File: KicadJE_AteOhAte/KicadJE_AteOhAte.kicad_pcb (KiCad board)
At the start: 2 copper layers, 100 x 100 mm, 180 parts, among them J201 In_Accent, J202 In Gate, J203 Out Tom, J301 Out 1, J302 In_1, J303 Out 2, J304 In 2, J305 Out 1 Final, J306 Out 2 Final, P201 Doepfer_Power_10pin, Q201 MMBT2222A, Q202 MMBT2222A, Q203 MMBT2222A, Q204 MMBT2222A, Q205 MMBT2907A, Q206 MMBT2222A, Q207 MMBT2222A, SW201 Con/Tom, U201 TL072, U202 TL072, U203 TL072, U301 TL072, U302 TL072

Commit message: PCB
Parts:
- removed C313, C314: 1u, Capacitor_SMD:C_0805_2012Metric_Pad1.15x1.40mm_HandSolder
- removed D311, D312: D_Zener, Diode_SMD:D_MiniMELF
- removed J301: Out 1, AJ-Dropbox-Kicad:PJ301SM
- removed J302: In_1, AJ-Dropbox-Kicad:PJ301SM
- removed J303: Out 2, AJ-Dropbox-Kicad:PJ301SM
- removed J304: In 2, AJ-Dropbox-Kicad:PJ301SM
- removed J305: Out 1 Final, AJ-Dropbox-Kicad:PJ301SM
- removed J306: Out 2 Final, AJ-Dropbox-Kicad:PJ301SM
- added H203: 2,2mm, MountingHole:MountingHole_2.2mm_M2_Pad_Via, F.Cu at (160.0, 53.5)
- D204: value Zener -> D_Zener
- moved D306 46.8 mm to (144.0, 33.9)
- moved D305 46.1 mm to (137.7, 33.9)
- moved C305 45.9 mm to (173.0, 52.0)
- moved R310 44.5 mm to (153.9, 39.5)
- moved R301 43.3 mm to (154.3, 33.6)
- moved D303 41.6 mm to (142.5, 38.3)
- moved C307 40.8 mm to (177.7, 52.0)
- moved C306 38.1 mm to (160.3, 24.2)
- moved C310 36.1 mm to (136.9, 40.2)
- moved R317 33.8 mm to (163.8, 33.0)
- moved R325 33.3 mm to (168.1, 36.0)
- moved D304 32.9 mm to (148.4, 21.6)
- moved C308 30.6 mm to (124.2, 44.7)
- moved R312 30.6 mm to (129.0, 44.7)
- moved U302 30.5 mm to (139.9, 20.6)
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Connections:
- net /KicadJE_AteOhAte3/POT1_C renamed Net-(R301-Pad2)
- net /KicadJE_AteOhAte3/POT1_L renamed Net-(C301-Pad1)
- net /KicadJE_AteOhAte3/POT2_L renamed Net-(R303-Pad1)
- net /KicadJE_AteOhAte3/POT3_C renamed Net-(R312-Pad1)
- net /KicadJE_AteOhAte3/POT4_C renamed Net-(R319-Pad2)
- C305 pad 1: Net-(C305-Pad1) -> (no net)
- C305 pad 2: Out1_Dist -> (no net)
- C306 pad 2: In_1 -> (no net)
- C307 pad 1: Net-(C307-Pad1) -> (no net)
- C307 pad 2: Out2_Dist -> (no net)
- C310 pad 2: In_2 -> (no net)
- R307 pad 2: In_1 -> (no net)
- R311 pad 2: Out1_Dist -> (no net)
- R317 pad 2: In_2 -> (no net)
- R322 pad 2: Out2_Dist -> (no net)
- R327 pad 1: Net-(J302-PadT) -> (no net)
- R329 pad 1: Net-(J302-PadTN) -> (no net)

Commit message: Fused RIAA SCH
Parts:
- removed D303, D310: LED, LED_THT:LED_D3.0mm
- removed D305, D306, D307, D308, D309: LL4148, Diode_SMD:D_MiniMELF
- added C313: 470n, Capacitor_SMD:C_0805_2012Metric_Pad1.15x1.40mm_HandSolder, B.Cu at (208.3, 122.9)
- added C314: 470n_THT, Capacitor_THT:C_Rect_L7.2mm_W5.5mm_P5.00mm_FKS2_FKP2_MKS2_MKP2, F.Cu at (182.0, 87.3)
- added C315: 470n_THT, Capacitor_THT:C_Rect_L7.2mm_W5.5mm_P5.00mm_FKS2_FKP2_MKS2_MKP2, F.Cu at (186.2, 50.8)
- added C316: 100u, Capacitor_SMD:CP_Elec_8x6.5, F.Cu at (158.0, 66.0)
- added C317: 2n2_THT, Capacitor_THT:C_Rect_L7.2mm_W5.5mm_P5.00mm_FKS2_FKP2_MKS2_MKP2, F.Cu at (189.1, 60.7)
- added C318: 47p, Capacitor_SMD:C_0805_2012Metric_Pad1.15x1.40mm_HandSolder, B.Cu at (202.7, 110.8)
- added C319: 2n2, Capacitor_SMD:C_0805_2012Metric_Pad1.15x1.40mm_HandSolder, B.Cu at (226.6, 134.5)
- added C320: 1n_THT, Capacitor_THT:C_Rect_L7.2mm_W5.5mm_P5.00mm_FKS2_FKP2_MKS2_MKP2, F.Cu at (164.5, 87.3)
- added C321: 680p_THT, Capacitor_THT:C_Rect_L7.2mm_W5.5mm_P5.00mm_FKS2_FKP2_MKS2_MKP2, F.Cu at (199.8, 52.9)
- added C322: 47p, Capacitor_SMD:C_0805_2012Metric_Pad1.15x1.40mm_HandSolder, B.Cu at (183.7, 111.7)
- added C323: 1n, Capacitor_SMD:C_0805_2012Metric_Pad1.15x1.40mm_HandSolder, B.Cu at (188.5, 110.7)
- added C324: 680p, Capacitor_SMD:C_0805_2012Metric_Pad1.15x1.40mm_HandSolder, B.Cu at (193.2, 113.6)
- added C325: 470n_THT, Capacitor_THT:C_Rect_L7.2mm_W5.5mm_P5.00mm_FKS2_FKP2_MKS2_MKP2, F.Cu at (208.6, 52.9)
- added C326: 470n, Capacitor_SMD:C_1206_3216Metric_Pad1.42x1.75mm_HandSolder, B.Cu at (192.4, 123.2)
- added C327: 470n, Capacitor_SMD:C_0805_2012Metric_Pad1.15x1.40mm_HandSolder, B.Cu at (212.4, 132.5)
- added C328: 470n, Capacitor_SMD:C_0805_2012Metric_Pad1.15x1.40mm_HandSolder, B.Cu at (198.8, 120.4)
- added C329: 470n_THT, Capacitor_THT:C_Rect_L7.2mm_W5.5mm_P5.00mm_FKS2_FKP2_MKS2_MKP2, F.Cu at (197.9, 60.7)
- added C330: 470n_THT, Capacitor_THT:C_Rect_L7.2mm_W5.5mm_P5.00mm_FKS2_FKP2_MKS2_MKP2, F.Cu at (167.4, 52.5)
- added C331: 10u, Capacitor_THT:CP_Radial_D8.0mm_P3.50mm, F.Cu at (184.8, 74.8)
- added C332: 22u, Capacitor_THT:CP_Radial_D8.0mm_P3.50mm, F.Cu at (163.8, 75.2)
- added C333: 10u, Capacitor_SMD:C_0805_2012Metric_Pad1.15x1.40mm_HandSolder, B.Cu at (221.9, 143.4)
- added C334: 1u, Capacitor_SMD:C_0805_2012Metric_Pad1.15x1.40mm_HandSolder, B.Cu at (202.5, 125.5)
- added C335: 100n, Capacitor_SMD:C_0805_2012Metric_Pad1.15x1.40mm_HandSolder, B.Cu at (177.4, 108.5)
- added C336: 100n, Capacitor_SMD:C_0805_2012Metric_Pad1.15x1.40mm_HandSolder, B.Cu at (212.4, 135.5)
- added C337: 100n, Capacitor_SMD:C_0805_2012Metric_Pad1.15x1.40mm_HandSolder, B.Cu at (188.5, 113.6)
- added C338: 100n, Capacitor_SMD:C_0805_2012Metric_Pad1.15x1.40mm_HandSolder, B.Cu at (221.9, 146.3)
- added C339: 100n, Capacitor_SMD:C_0805_2012Metric_Pad1.15x1.40mm_HandSolder, B.Cu at (226.7, 149.3)
- added C340: 100n, Capacitor_SMD:C_0805_2012Metric_Pad1.15x1.40mm_HandSolder, B.Cu at (215.2, 138.5)
- added C341: 10u, Capacitor_SMD:C_0805_2012Metric_Pad1.15x1.40mm_HandSolder, B.Cu at (194.0, 117.1)
- added C342: 1u, Capacitor_SMD:C_0805_2012Metric_Pad1.15x1.40mm_HandSolder, B.Cu at (198.0, 111.6)
- added C343: 10u, Capacitor_THT:CP_Radial_D8.0mm_P3.50mm, F.Cu at (175.0, 75.2)
- added C344: 22u, Capacitor_THT:CP_Radial_D8.0mm_P3.50mm, F.Cu at (195.5, 75.5)
- added C345: 470u, Capacitor_THT:CP_Radial_D13.0mm_P5.00mm, F.Cu at (116.0, 65.5)
- added C346: 470u, Capacitor_THT:CP_Radial_D13.0mm_P5.00mm, F.Cu at (116.0, 79.0)
- added J301: PJRAS2X2S01AUX, AJ:PJRAS2X2S01AUX_RCA, F.Cu at (141.0, 119.8)
- added J302: Conn_01x03, TerminalBlock:TerminalBlock_bornier-3_P5.08mm, F.Cu at (105.0, 79.5)
- added U303: TL072, AJ-Dropbox-Kicad:AJ_SO-8_5.3x6.2mm_P1.27mm, B.Cu at (167.2, 116.5)
- C301: value 10n -> 2n2_THT; footprint Capacitor_SMD:C_0805_2012Metric_Pad1.15x1.40mm_HandSolder -> Capacitor_THT:C_Rect_L7.2mm_W5.5mm_P5.00mm_FKS2_FKP2_MKS2_MKP2
- C302: value 10n -> 100u; footprint Capacitor_SMD:C_0805_2012Metric_Pad1.15x1.40mm_HandSolder -> Capacitor_SMD:CP_Elec_8x6.5
- C303: value 10n -> 2n2; moved to B.Cu
- C304: value 10n -> 1n_THT; footprint Capacitor_SMD:C_0805_2012Metric_Pad1.15x1.40mm_HandSolder -> Capacitor_THT:C_Rect_L7.2mm_W5.5mm_P5.00mm_FKS2_FKP2_MKS2_MKP2
- C305: value 1u -> 680p_THT; footprint Capacitor_SMD:C_0805_2012Metric_Pad1.15x1.40mm_HandSolder -> Capacitor_THT:C_Rect_L7.2mm_W5.5mm_P5.00mm_FKS2_FKP2_MKS2_MKP2
- C306, C310: value 1u -> 47p; moved to B.Cu
- C307: value 1u -> 1n; moved to B.Cu
- C308: value 100n -> 680p; moved to B.Cu
- C309: value 100n -> 470n_THT; footprint Capacitor_SMD:C_0805_2012Metric_Pad1.15x1.40mm_HandSolder -> Capacitor_THT:C_Rect_L7.2mm_W5.5mm_P5.00mm_FKS2_FKP2_MKS2_MKP2
- C311: value 100n -> 470n; footprint Capacitor_SMD:C_0805_2012Metric_Pad1.15x1.40mm_HandSolder -> Capacitor_SMD:C_1206_3216Metric_Pad1.42x1.75mm_HandSolder; moved to B.Cu
- C312: value 100n -> 470n; moved to B.Cu
- D301, D302, H302, H304, U301, U302: moved to B.Cu
- D304: value LL4148 -> LED; footprint Diode_SMD:D_MiniMELF -> LED_THT:LED_D3.0mm
- R301: value 1k -> 220R; moved to B.Cu
- R302: value 10k -> 2k2; moved to B.Cu
- R303: value 10k -> 82k; moved to B.Cu
- R304, R305, R319: value 1k -> 2k2; moved to B.Cu
- R306, R311, R324: value 1k -> 470R; moved to B.Cu
- R307, R317, R318: value 10k -> 470R; moved to B.Cu
- R308, R312: value 10k -> 18k; moved to B.Cu
- R309, R323: value 10R -> 1M; moved to B.Cu
- R310: value 1k -> 47k; moved to B.Cu
- R313: value 100k -> 18k; moved to B.Cu
- R314: value 10k -> 220R; moved to B.Cu
- R315: value 100k -> 2k2; moved to B.Cu
- R316: value 1k -> 82k; moved to B.Cu
- R320: value Open -> 2k2; moved to B.Cu
- R321: value Open -> 47k; moved to B.Cu
- R322: value 1k -> 18k; moved to B.Cu
- R325: value 0R -> 18k; moved to B.Cu
- R326: value 0R -> 680k; moved to B.Cu
- R327: value 10k -> 12k; moved to B.Cu
- R328: value OPEN -> 680k; moved to B.Cu
- R329: value 10k -> 1R1; moved to B.Cu
- R330: value OPEN -> 1R1; moved to B.Cu
- moved C310 138.3 mm to (221.9, 149.3)
- moved R301 133.9 mm to (226.7, 146.3)
- moved R305 133.9 mm to (226.7, 143.4)
- moved U302 131.9 mm to (178.0, 146.9)
- moved C306 129.5 mm to (215.2, 141.4)
- moved U301 128.2 mm to (188.7, 146.9)
- moved H304 126.4 mm to (209.9, 139.9)
- moved R320 126.4 mm to (226.6, 137.5)
- moved R322 124.1 mm to (224.7, 140.4)
- moved R307 123.3 mm to (217.1, 135.5)
- moved R310 120.6 mm to (220.0, 140.4)
- moved R303 120.3 mm to (217.1, 132.6)
- moved C303 117.7 mm to (206.4, 128.8)
- moved R321 116.9 mm to (221.9, 134.5)
- moved C311 114.7 mm to (201.1, 134.2)
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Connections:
- C303 pad 1: Net-(C303-Pad1) -> Net-(C301-Pad1)
- C303 pad 2: Net-(C303-Pad2) -> Net-(C301-Pad2)
- C304 pad 1: Net-(C304-Pad1) -> Net-(C301-Pad2)
- C304 pad 2: GND -> Net-(C304-Pad2)
- C305 pad 1: (no net) -> Net-(C301-Pad1)
- C305 pad 2: (no net) -> Net-(C301-Pad2)
- C306 pad 2: (no net) -> Net-(C306-Pad2)
- C307 pad 1: (no net) -> Net-(C301-Pad2)
- C307 pad 2: (no net) -> Net-(C304-Pad2)
- C308 pad 1: GND -> Net-(C301-Pad1)
- C308 pad 2: +12V -> Net-(C301-Pad2)
- C309 pad 1: GND -> Net-(C309-Pad1)
- C309 pad 2: +12V -> L_Rumble_Out
- C310 pad 2: (no net) -> GND
- C311 pad 1: -12V -> Net-(C309-Pad1)
- C311 pad 2: GND -> L_Rumble_Out
- C312 pad 1: -12V -> Net-(C312-Pad1)
- C312 pad 2: GND -> L_GainOut
- D301 pad 1: Net-(C301-Pad2) -> (no net)
- D301 pad 2: Net-(C301-Pad1) -> (no net)
- D302 pad 1: Net-(C301-Pad1) -> (no net)
- D302 pad 2: Net-(C301-Pad2) -> (no net)
- D304 pad 1: Net-(C302-Pad1) -> /KicadJE_AteOhAte3/-PSU
- D304 pad 2: GND -> Net-(D304-Pad2)
- R301 pad 1: Net-(C301-Pad2) -> Net-(C306-Pad1)
- R301 pad 2: Net-(R301-Pad2) -> Net-(C302-Pad1)
- R302 pad 1: Net-(C301-Pad1) -> L_GainOut
- R302 pad 2: GND -> Net-(C306-Pad1)
- R303 pad 1: Net-(R303-Pad1) -> Net-(C301-Pad2)
- R303 pad 2: GND -> Net-(C304-Pad2)
- R304 pad 1: (no net) -> Net-(R304-Pad1)
- R304 pad 2: Net-(R304-Pad2) -> GND
- R305 pad 1: Net-(R301-Pad2) -> L_Rumble_Out
- R305 pad 2: Net-(R305-Pad2) -> Net-(R304-Pad1)
- R306 pad 1: Out1_Final -> Net-(C310-Pad1)
- R306 pad 2: Net-(R304-Pad2) -> In_L
- R307 pad 1: Net-(R307-Pad1) -> Net-(C306-Pad2)
- R307 pad 2: (no net) -> Net-(C310-Pad1)
- R308 pad 1: Net-(R308-Pad1) -> Net-(C304-Pad2)
- R308 pad 2: Net-(R305-Pad2) -> Net-(C309-Pad1)
- R309 pad 1: Net-(C302-Pad1) -> Net-(C301-Pad1)
- R309 pad 2: Out1_Final -> Net-(C304-Pad2)
- R310 pad 1: Net-(D303-Pad2) -> GND
- R310 pad 2: Net-(R304-Pad2) -> Net-(C310-Pad1)
- R311 pad 1: Net-(R305-Pad2) -> Out_L
- R311 pad 2: (no net) -> Net-(C301-Pad1)
- R312 pad 1: Net-(R312-Pad1) -> L_Rumble_Out
- R312 pad 2: Net-(C303-Pad2) -> Net-(C312-Pad1)
- R313 pad 1: Net-(R313-Pad1) -> GND
- R313 pad 2: GND -> Net-(C313-Pad1)
- R314 pad 1: (no net) -> Net-(C318-Pad1)
- R314 pad 2: Net-(R313-Pad1) -> Net-(C316-Pad1)
- R315 pad 1: Net-(C303-Pad1) -> R_GainOut
- R315 pad 2: GND -> Net-(C318-Pad1)
- R316 pad 1: (no net) -> Net-(C317-Pad2)
- R316 pad 2: Net-(C303-Pad1) -> Net-(C320-Pad2)
- R317 pad 1: Net-(C303-Pad1) -> Net-(C322-Pad1)
- R317 pad 2: (no net) -> In_R
- R318 pad 1: Net-(R313-Pad1) -> Net-(C318-Pad2)
- R318 pad 2: Net-(R312-Pad1) -> Net-(C322-Pad1)
- R319 pad 1: Out2_Final -> Net-(R319-Pad1)
- R319 pad 2: Net-(R319-Pad2) -> GND
- R320 pad 1: Net-(R320-Pad1) -> R_Rumble_Out
- R320 pad 2: +12V -> Net-(R319-Pad1)
- R321 pad 1: Net-(R321-Pad1) -> GND
- R321 pad 2: +12V -> Net-(C322-Pad1)
- R322 pad 1: Net-(R312-Pad1) -> Net-(C320-Pad2)
- R322 pad 2: (no net) -> Net-(C325-Pad1)
- R323 pad 1: Net-(C304-Pad1) -> Net-(C317-Pad1)
- R323 pad 2: Out2_Final -> Net-(C320-Pad2)
- R324 pad 1: Net-(D310-Pad2) -> Out_R
- R324 pad 2: Net-(R319-Pad2) -> Net-(C317-Pad1)
- R325 pad 1: GND -> R_Rumble_Out
- R325 pad 2: Net-(R320-Pad1) -> Net-(C327-Pad1)
- R326 pad 1: GND -> Net-(C331-Pad2)
- R326 pad 2: Net-(R321-Pad1) -> GND
- R327 pad 1: (no net) -> Net-(D304-Pad2)
- R327 pad 2: Net-(C306-Pad1) -> /KicadJE_AteOhAte3/+PSU
- R328 pad 1: Net-(C306-Pad1) -> GND
- R328 pad 2: GND -> Net-(C341-Pad1)
- R329 pad 1: (no net) -> +12V
- R329 pad 2: Net-(C310-Pad1) -> /KicadJE_AteOhAte3/+PSU
- R330 pad 1: Net-(C310-Pad1) -> -12V
- R330 pad 2: GND -> /KicadJE_AteOhAte3/-PSU
- U301 pad 1: Net-(R304-Pad2) -> L_GainOut
- U301 pad 2: Net-(R303-Pad1) -> Net-(C306-Pad1)
- U301 pad 3: Net-(R308-Pad1) -> Net-(C306-Pad2)
- U301 pad 5: Net-(R307-Pad1) -> Net-(C318-Pad2)
- U301 pad 6: Net-(C301-Pad1) -> Net-(C318-Pad1)
- U301 pad 7: Net-(R305-Pad2) -> R_GainOut
- U302 pad 1: Net-(R319-Pad2) -> L_Rumble_Out
- U302 pad 2: Net-(R313-Pad1) -> Net-(R304-Pad1)
- U302 pad 3: Net-(R321-Pad1) -> Net-(C313-Pad1)
- U302 pad 5: Net-(R320-Pad1) -> Net-(C328-Pad1)
- U302 pad 6: Net-(C303-Pad1) -> Net-(R319-Pad1)
- U302 pad 7: Net-(R312-Pad1) -> R_Rumble_Out

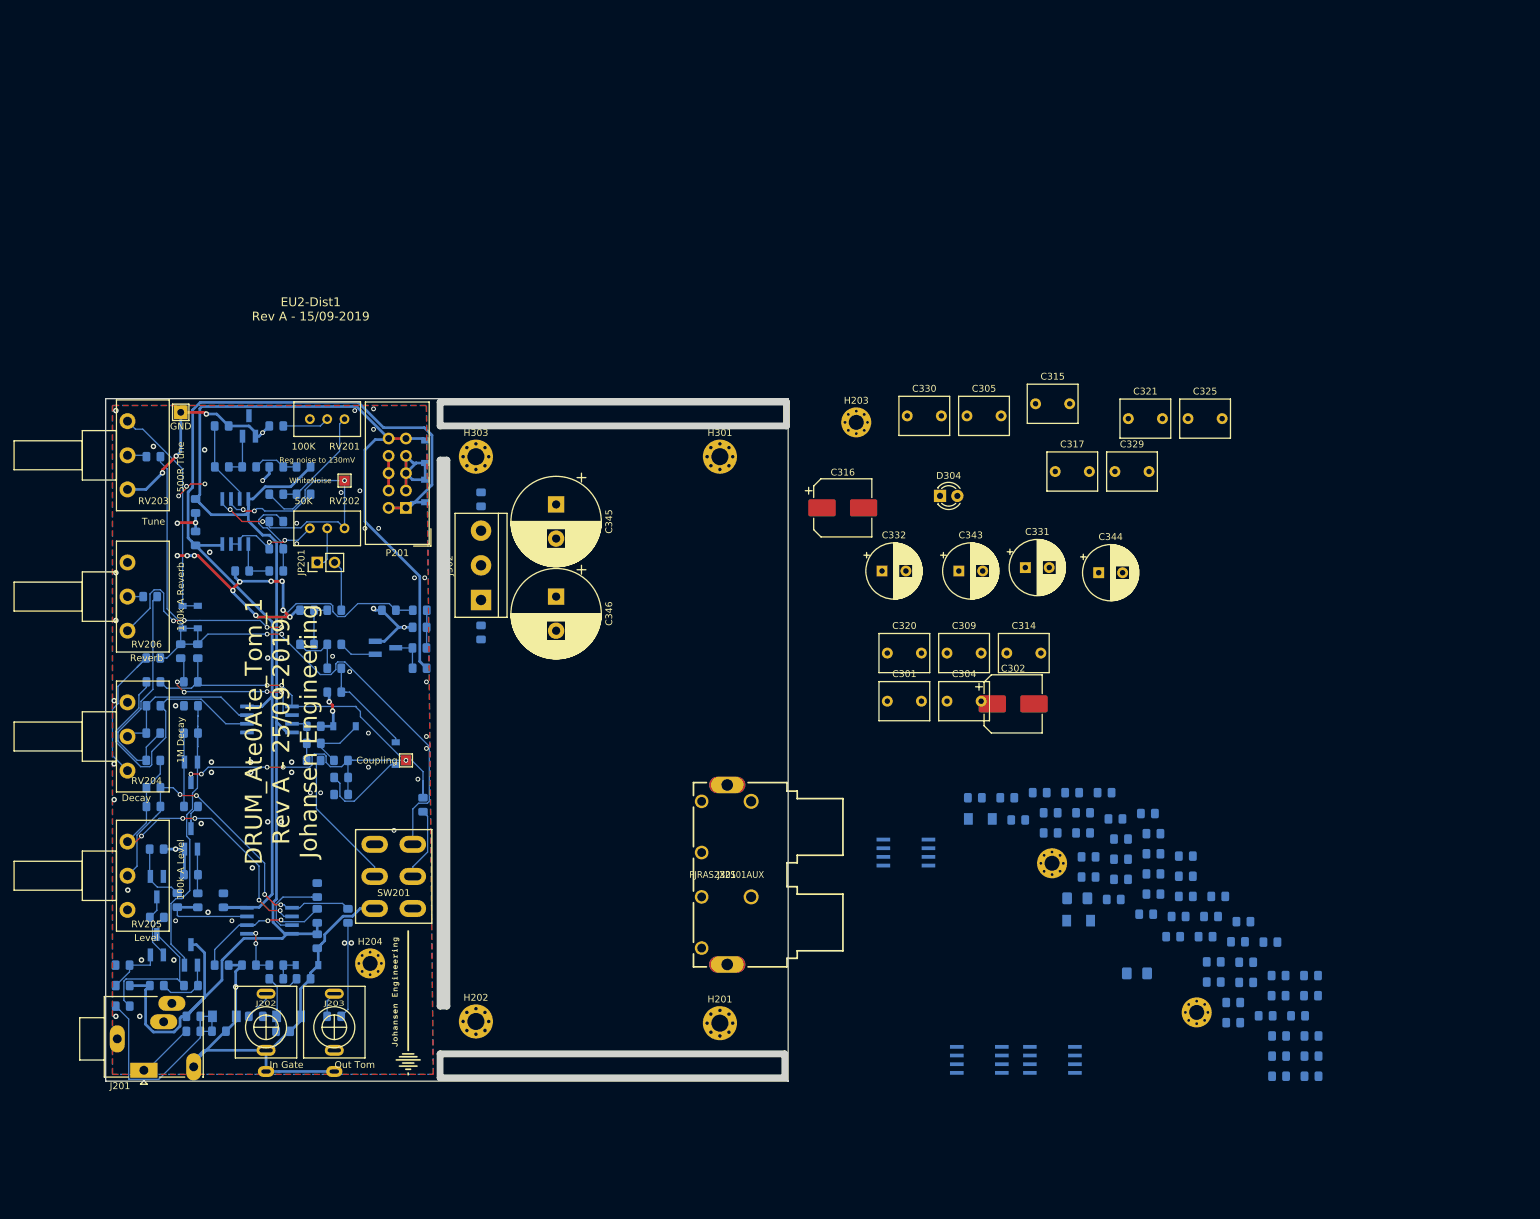
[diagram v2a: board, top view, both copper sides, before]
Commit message: RIAA Basic THT placed
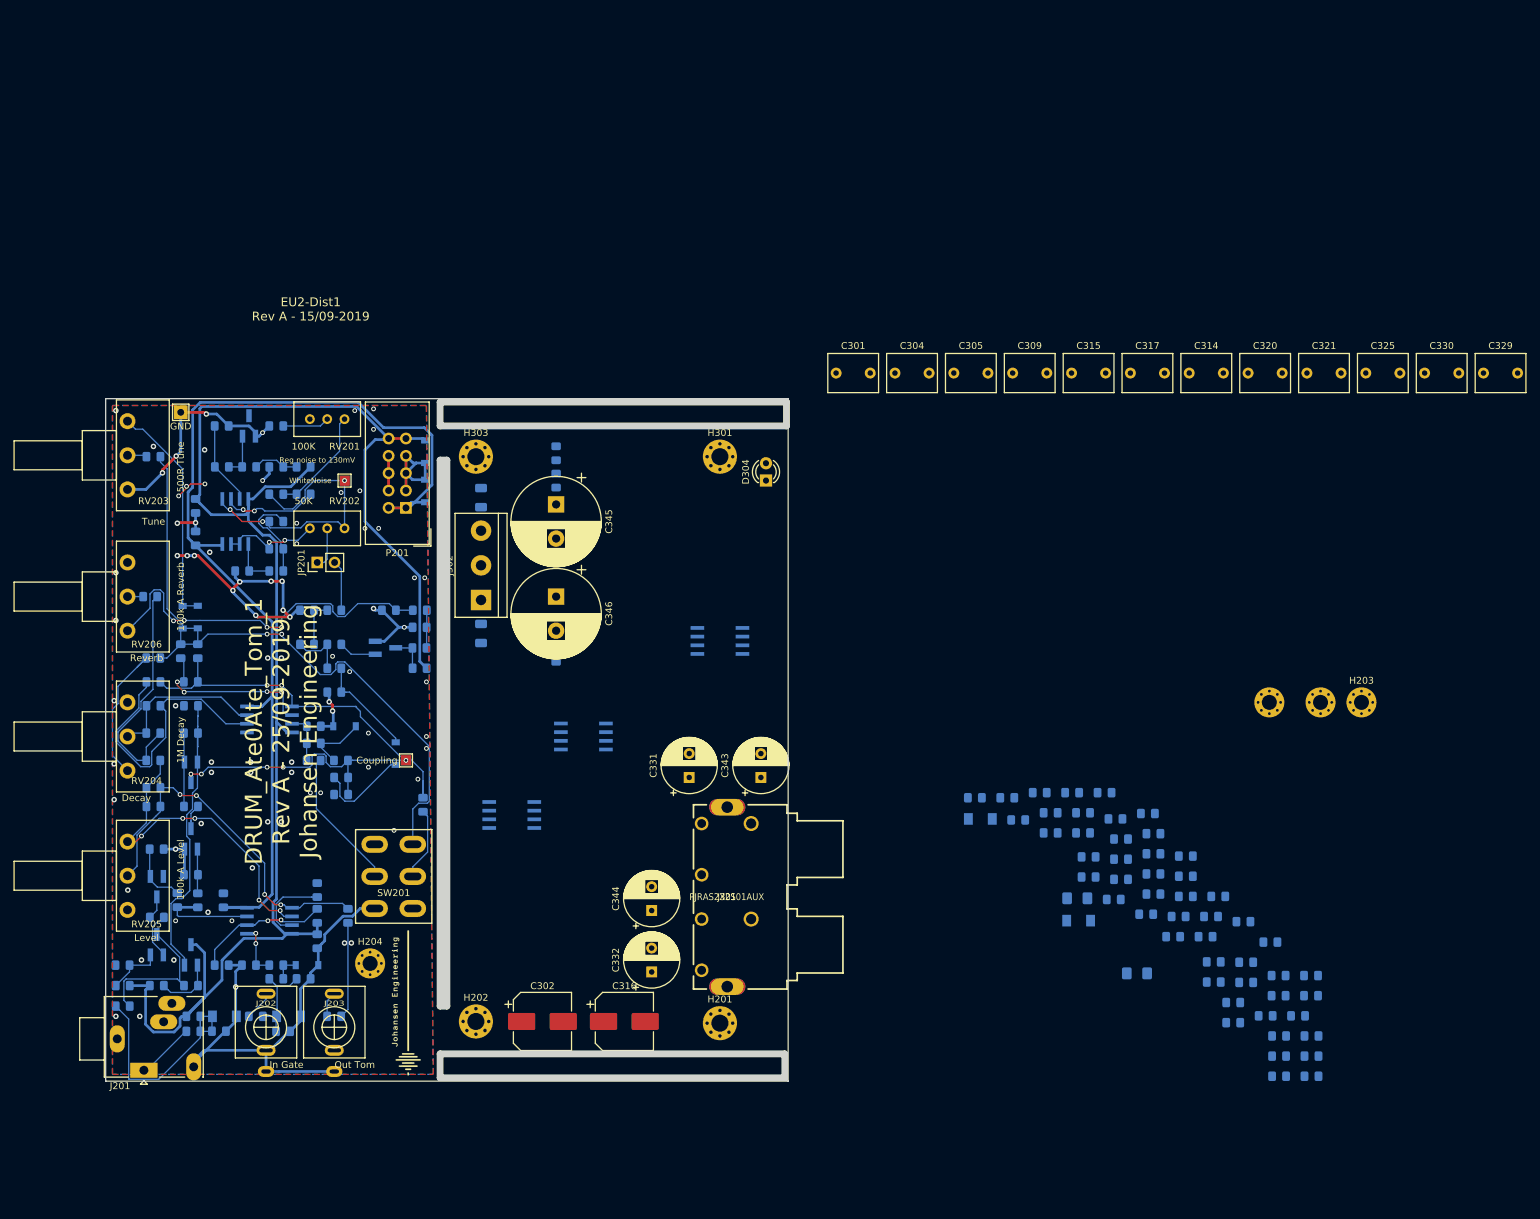
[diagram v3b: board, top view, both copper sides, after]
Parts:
- added F301: Polyfuse, Fuse:Fuse_1206_3216Metric, B.Cu at (105.0, 64.5)
- added F302: Polyfuse, Fuse:Fuse_1206_3216Metric, B.Cu at (105.0, 84.4)
- moved R327 122.9 mm to (116.0, 58.0), turned to 270 degrees
- moved H203 84.6 mm to (234.0, 94.5)
- moved C302 83.2 mm to (114.0, 141.2)
- moved C344 82.1 mm to (130.0, 125.0), turned to 90 degrees
- moved C316 81.8 mm to (126.0, 141.2)
- moved U301 78.4 mm to (140.0, 85.5)
- moved C330 76.1 mm to (243.3, 46.2)
- moved U302 74.9 mm to (120.0, 99.5)
- moved C332 67.8 mm to (130.0, 134.0), turned to 90 degrees
- moved C320 66.9 mm to (217.4, 46.2)
- moved C331 58.1 mm to (135.5, 105.5), turned to 90 degrees
- moved U303 58.0 mm to (109.5, 111.0)
- moved C329 55.9 mm to (251.9, 46.2)
- moved C314 49.0 mm to (208.8, 46.2)
- moved C304 48.7 mm to (165.6, 46.2)
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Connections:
- D304 pad 1: /KicadJE_AteOhAte3/-PSU -> Net-(D304-Pad1)
- J302 pad 2: GND -> (no net)
- R327 pad 1: Net-(D304-Pad2) -> Net-(F301-Pad2)
- R327 pad 2: /KicadJE_AteOhAte3/+PSU -> Net-(D304-Pad2)
- R329 pad 2: /KicadJE_AteOhAte3/+PSU -> Net-(F301-Pad2)
- R330 pad 2: /KicadJE_AteOhAte3/-PSU -> Net-(D304-Pad1)

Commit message: RIAA decoupling
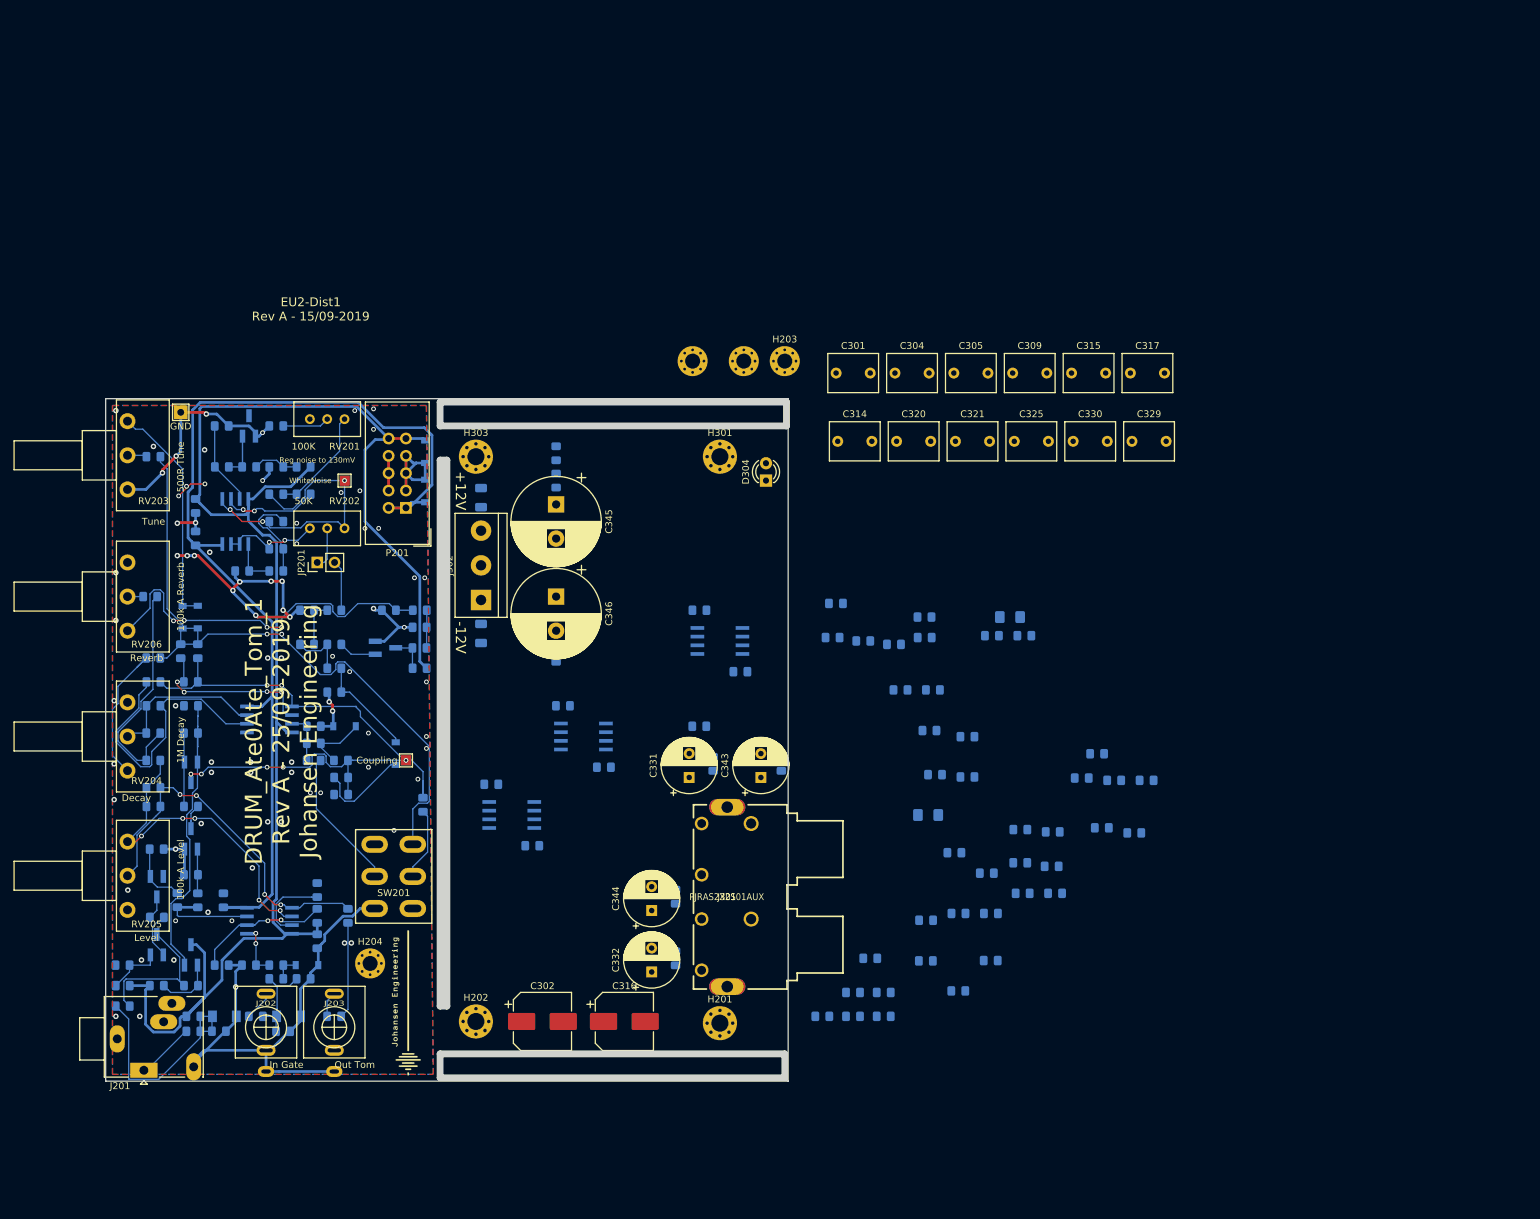
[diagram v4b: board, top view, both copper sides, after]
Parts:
- removed D301, D302: LL4148, Diode_SMD:D_MiniMELF
- moved C339 122.4 mm to (117.0, 95.0)
- moved C338 122.1 mm to (106.5, 106.5)
- moved C336 101.8 mm to (112.5, 115.5)
- moved H203 98.2 mm to (149.5, 44.5)
- moved H302 98.2 mm to (143.5, 44.5)
- moved H304 98.2 mm to (136.0, 44.5)
- moved C340 97.1 mm to (137.0, 81.0)
- moved C333 92.0 mm to (139.0, 103.5), turned to 270 degrees
- moved R321 71.7 mm to (170.0, 85.0)
- moved R317 69.5 mm to (170.0, 82.0)
- moved C334 69.3 mm to (133.5, 132.0), turned to 270 degrees
- moved R326 69.1 mm to (137.0, 98.0)
- moved C337 66.2 mm to (123.0, 104.0)
- moved C342 65.5 mm to (133.5, 123.0), turned to 270 degrees
- moved R305 57.6 mm to (170.2, 132.4)
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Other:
- board text added: "+12V"
- board text added: "-12V"
